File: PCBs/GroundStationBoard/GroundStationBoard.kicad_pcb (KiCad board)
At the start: 2 copper layers, 0 parts

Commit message: 4 layer-ifying the PCB, traces, board cuts and trace width
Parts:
- added A1: ADA3708, ADA3708:ADA3708_RPI-ZERO, F.Cu at (211.0, 52.0)
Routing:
- added copper zone on In2.Cu, net +5V
- added copper zone on B.Cu, net GND
- added copper zone on In1.Cu, net GND
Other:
- board outline added: 100 x 100 mm
- copper layers 2 -> 4

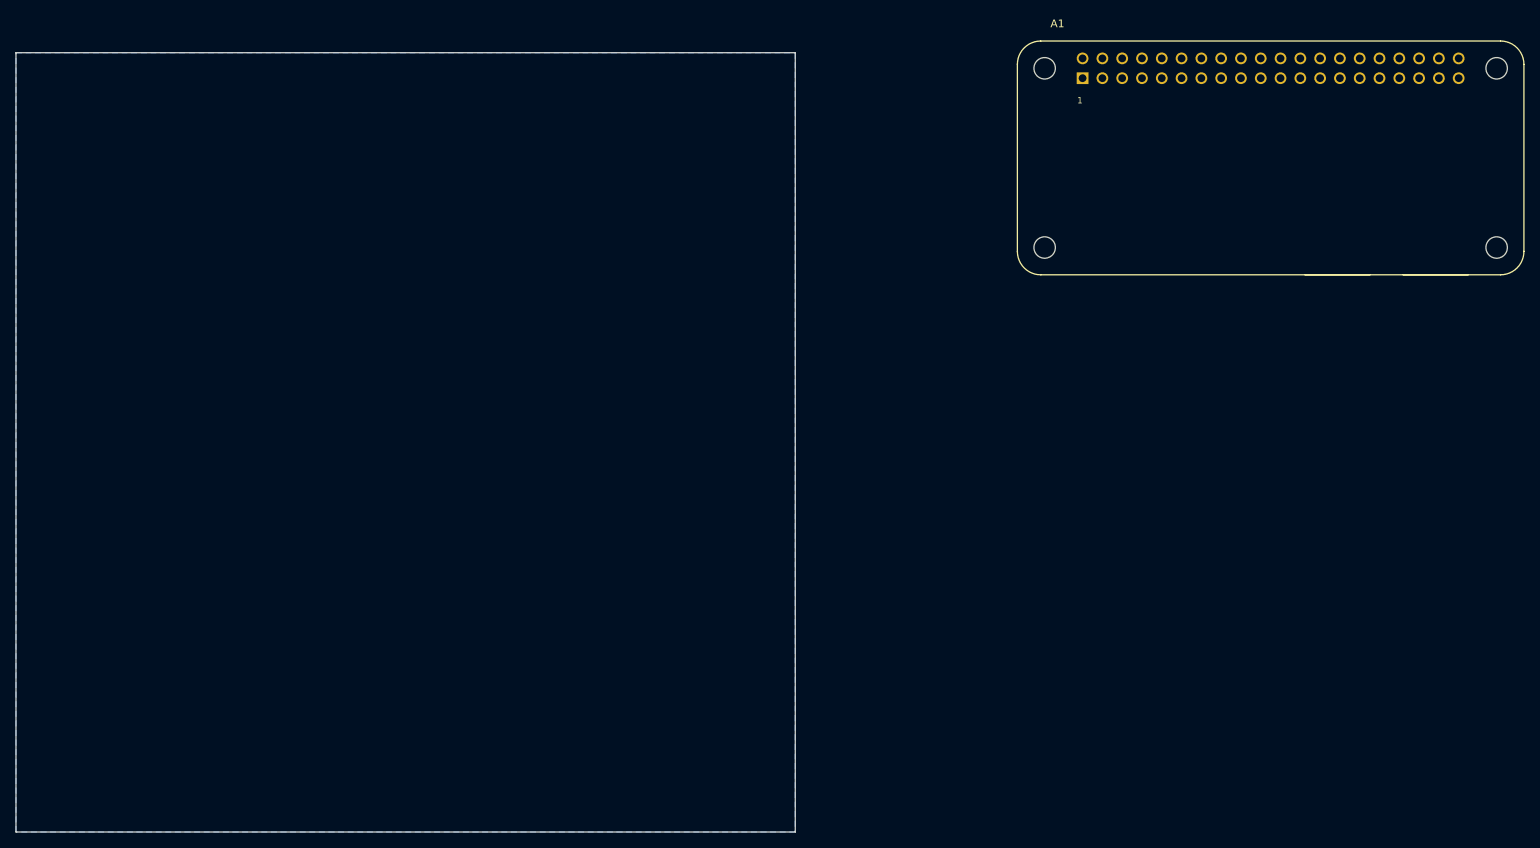
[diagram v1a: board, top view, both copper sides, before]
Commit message: added SMA connector and RF switch to schematic
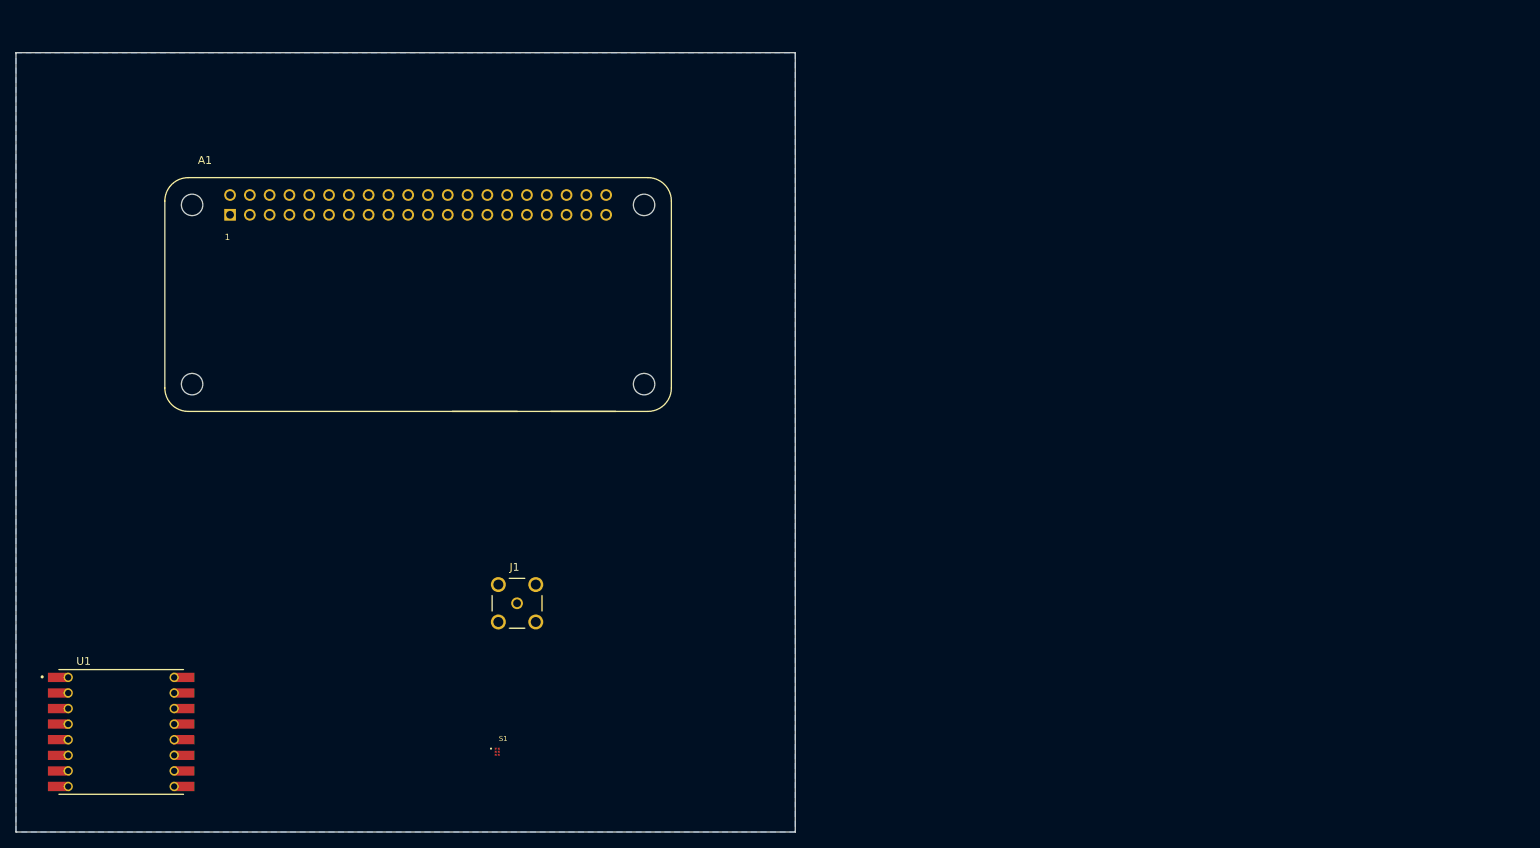
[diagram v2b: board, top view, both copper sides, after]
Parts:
- added J1: SMA_CONNECTOR, SMA_CONNECTOR:LPRS_SMA_CONNECTOR, F.Cu at (114.3, 120.7)
- added S1: BGS12P2L6E6327XTSA1, BGS12P2L6E6327XTSA1:SW_BGS12P2L6E6327XTSA1, F.Cu at (111.8, 139.7)
- added U1: RFM98W, RFM98W-433S2:XCVR_RFM98W-433S2, F.Cu at (63.5, 137.2)
- A1: value ADA3708 -> Raspberry Pi Zero
- moved A1 110.8 mm to (101.6, 69.5)
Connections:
- A1 pad 19: unconnected-(A1-Pad19) -> MOSI
- A1 pad 21: unconnected-(A1-Pad21) -> MISO
- A1 pad 23: unconnected-(A1-Pad23) -> SCLK
- A1 pad 24: unconnected-(A1-Pad24) -> CS
- A1 pad 40: unconnected-(A1-Pad40) -> RST

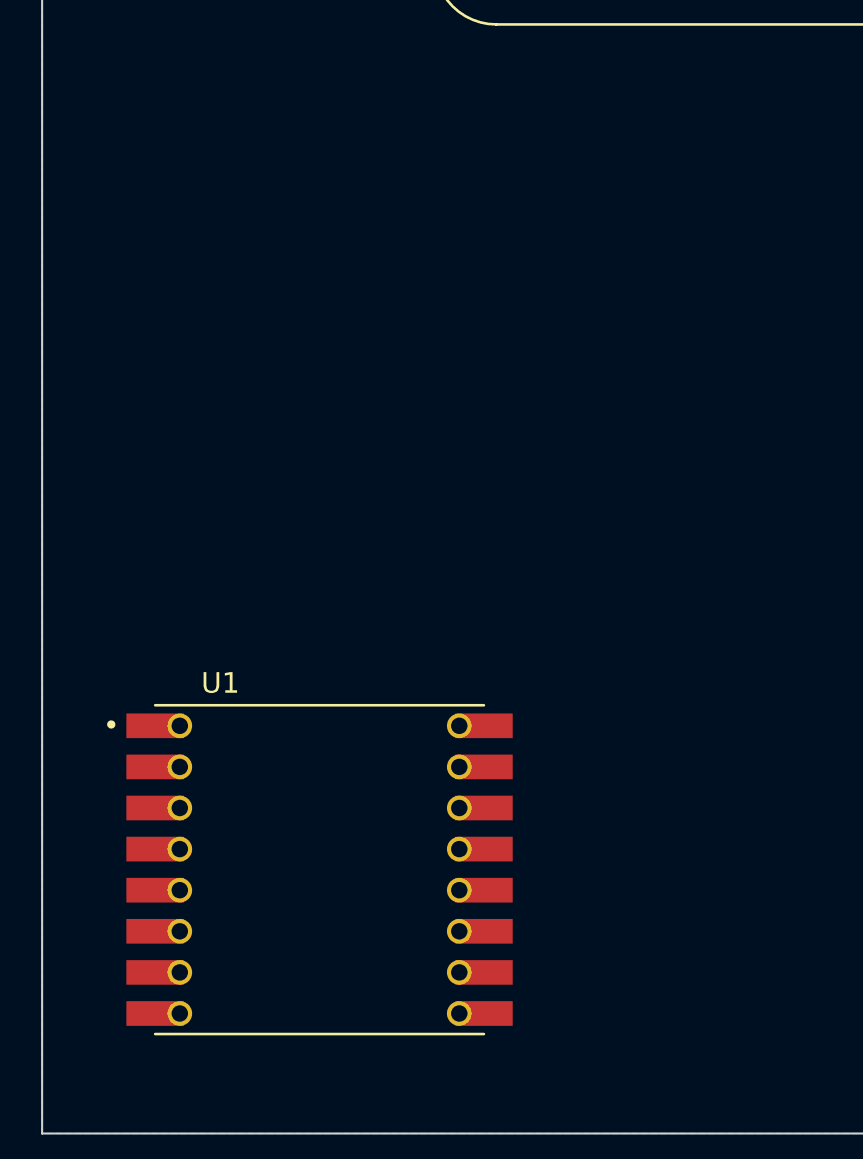
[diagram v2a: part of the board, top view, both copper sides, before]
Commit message: worked on data I/O pins
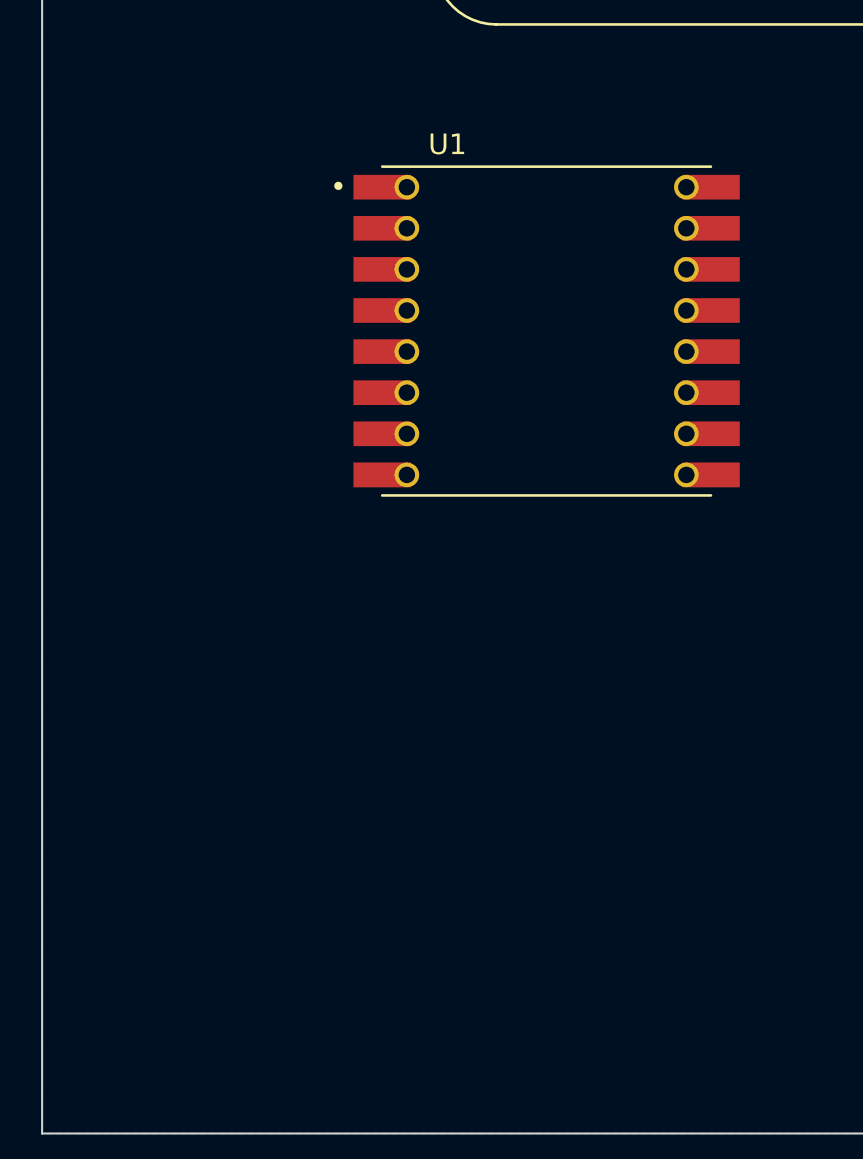
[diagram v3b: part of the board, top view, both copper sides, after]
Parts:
- moved U1 28.4 mm to (74.5, 111.0)
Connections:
- A1 pad 11: unconnected-(A1-Pad11) -> RST
- A1 pad 13: unconnected-(A1-Pad13) -> SWCH
- A1 pad 33: unconnected-(A1-Pad33) -> DIO0
- A1 pad 35: unconnected-(A1-Pad35) -> DIO1
- A1 pad 36: unconnected-(A1-Pad36) -> DIO3
- A1 pad 37: unconnected-(A1-Pad37) -> DIO2
- A1 pad 38: unconnected-(A1-Pad38) -> DIO4
- A1 pad 40: RST -> DIO5
- S1 pad 1: unconnected-(S1-Pad1) -> AMP
- S1 pad 3: unconnected-(S1-Pad3) -> ANT
- S1 pad 5: unconnected-(S1-Pad5) -> RF
- S1 pad 6: unconnected-(S1-Pad6) -> SWCH
- U1 pad 11: unconnected-(U1-Pad11) -> DIO3
- U1 pad 12: unconnected-(U1-Pad12) -> DIO4
- U1 pad 14: unconnected-(U1-Pad14) -> DIO0
- U1 pad 15: unconnected-(U1-Pad15) -> DIO1
- U1 pad 16: unconnected-(U1-Pad16) -> DIO2
- U1 pad 7: unconnected-(U1-Pad7) -> DIO5
- U1 pad 9: ANT -> RF

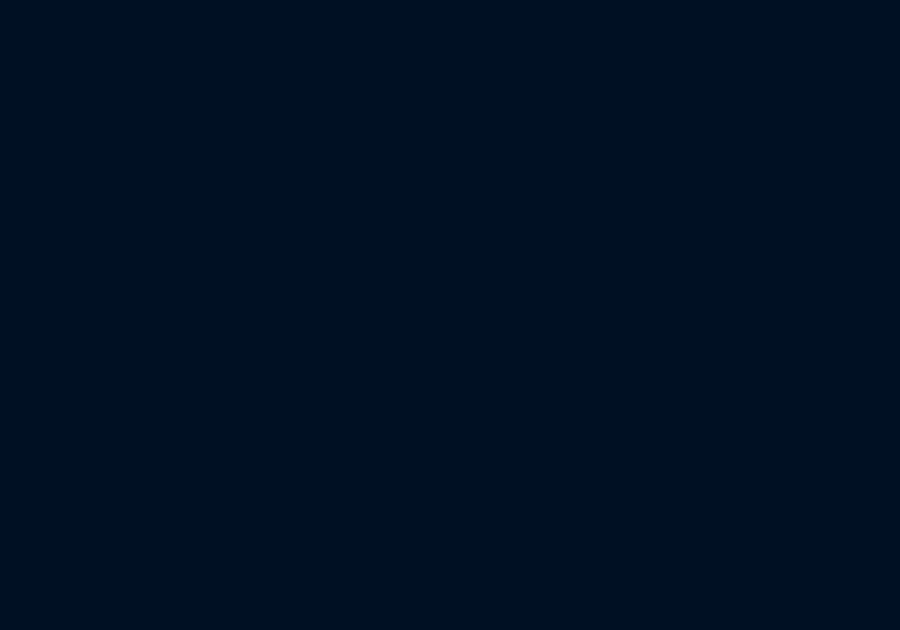
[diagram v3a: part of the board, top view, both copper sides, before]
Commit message: added amplifier
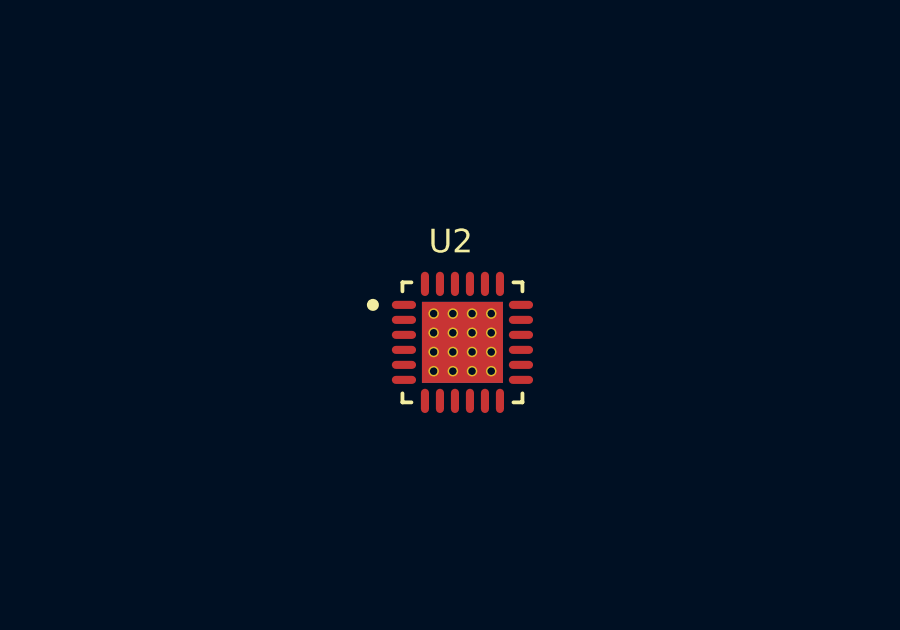
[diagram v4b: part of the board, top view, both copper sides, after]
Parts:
- added U2: TQP7M9106, TQP7M9106:QFN50P400X400X90-25N, F.Cu at (82.5, 135.9)
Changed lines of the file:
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@@
   (net 33 "DIO4")
   (net 34 "DIO5")
+  (net 35 "Net-(U2-Pad10)")
+  (net 36 "unconnected-(U2-Pad1)")
+  (net 37 "Net-(U2-Pad4)")
+  (net 38 "Net-(U2-Pad14)")
+  (net 39 "unconnected-(U2-Pad18)")
+  (net 40 "Net-(U2-Pad25)")
   (footprint "RFM98W-433S2:XCVR_RFM98W-433S2" (layer "F.Cu")
     (at 74.55 110.95)
@@
       (net 5 "GND") (pintype "passive"))
   )
+  (footprint "TQP7M9106:QFN50P400X400X90-25N" (layer "F.Cu")
+    (at 82.55 135.89)
+    (property "MANUFACTURER" "Qorvo")
+    (property "MAXIMUM_PACKAGE_HEIGHT" "0.9 mm")
+    (property "PARTREV" "Rev.D")
+    (property "SNAPEDA_PN" "TQP7M9106")
+    (property "STANDARD" "IPC-7351B")
+    (property "Sheetfile" "GroundStationBoard.kicad_sch")
+    (property "Sheetname" "")
+    (attr through_hole)
+    (fp_text reference "U2" (at -0.39 -3.365) (layer "F.SilkS")
+      (effects (font (size 0.787402 0.787402) (thickness 0.15)))
+    )
+    (fp_text value "TQP7M9106" (at 7.11 3.365) (layer "F.Fab")
+      (effects (font (size 0.787402 0.787402) (thickness 0.15)))
+    )
+    (fp_poly (pts
+        (xy -0.85 -0.85)
+        (xy 0.85 -0.85)
+        (xy 0.85 0.85)
+        (xy -0.85 0.85)
+      ) (layer "F.Paste") (width 0.01) (fill solid))
+    (fp_line (start -2 -2) (end -1.7 -2) (layer "F.SilkS") (width 0.127))
+    (fp_line (start 2 2) (end 1.7 2) (layer "F.SilkS") (width 0.127))
+    (fp_line (start -2 -2) (end -2 -1.7) (layer "F.SilkS") (width 0.127))
+    (fp_line (start 2 -2) (end 2 -1.7) (layer "F.SilkS") (width 0.127))
+    (fp_line (start -2 2) (end -1.7 2) (layer "F.SilkS") (width 0.127))
+    (fp_line (start -2 2) (end -2 1.7) (layer "F.SilkS") (width 0.127))
+    (fp_line (start 2 2) (end 2 1.7) (layer "F.SilkS") (width 0.127))
+    (fp_line (start 2 -2) (end 1.7 -2) (layer "F.SilkS") (width 0.127))
+    (fp_circle (center -2.985 -1.25) (end -2.885 -1.25) (layer "F.SilkS") (width 0.2) (fill none))
+    (fp_line (start 2.615 2.615) (end 2.615 -2.615) (layer "F.CrtYd") (width 0.05))
+    (fp_line (start -2.615 -2.615) (end 2.615 -2.615) (layer "F.CrtYd") (width 0.05))
+    (fp_line (start -2.615 2.615) (end -2.615 -2.615) (layer "F.CrtYd") (width 0.05))
+    (fp_line (start -2.615 2.615) (end 2.615 2.615) (layer "F.CrtYd") (width 0.05))
+    (fp_line (start 2 2) (end -2 2) (layer "F.Fab") (width 0.127))
+    (fp_line (start 2 2) (end 2 -2) (layer "F.Fab") (width 0.127))
+    (fp_line (start -2 2) (end -2 -2) (layer "F.Fab") (width 0.127))
+    (fp_line (start 2 -2) (end -2 -2) (layer "F.Fab") (width 0.127))
+    (fp_circle (center -2.985 -1.25) (end -2.885 -1.25) (layer "F.Fab") (width 0.2) (fill none))
+    (pad "1" smd oval locked (at -1.95 -1.25) (size 0.81 0.27) (layers "F.Cu" "F.Paste" "F.Mask")
+      (net 36 "unconnected-(U2-Pad1)") (pinfunction "VBIAS") (pintype "power_in"))
+    (pad "2" smd oval locked (at -1.95 -0.75) (size 0.81 0.27) (layers "F.Cu" "F.Paste" "F.Mask")
+      (net 35 "Net-(U2-Pad10)") (pinfunction "GND/NC") (pintype "power_in"))
+    (pad "3" smd oval locked (at -1.95 -0.25) (size 0.81 0.27) (layers "F.Cu" "F.Paste" "F.Mask")
+      (net 35 "Net-(U2-Pad10)") (pinfunction "GND/NC") (pintype "power_in"))
+    (pad "4" smd oval locked (at -1.95 0.25) (size 0.81 0.27) (layers "F.Cu" "F.Paste" "F.Mask")
+      (net 37 "Net-(U2-Pad4)") (pinfunction "RF_IN") (pintype "input"))
+    (pad "5" smd oval locked (at -1.95 0.75) (size 0.81 0.27) (layers "F.Cu" "F.Paste" "F.Mask")
+      (net 37 "Net-(U2-Pad4)") (pinfunction "RF_IN") (pintype "input"))
+    (pad "6" smd oval locked (at -1.95 1.25) (size 0.81 0.27) (layers "F.Cu" "F.Paste" "F.Mask")
+      (net 35 "Net-(U2-Pad10)") (pinfunction "GND/NC") (pintype "power_in"))
+    (pad "7" smd oval locked (at -1.25 1.95) (size 0.27 0.81) (layers "F.Cu" "F.Paste" "F.Mask")
+      (net 35 "Net-(U2-Pad10)") (pinfunction "GND/NC") (pintype "power_in"))
+    (pad "8" smd oval locked (at -0.75 1.95) (size 0.27 0.81) (layers "F.Cu" "F.Paste" "F.Mask")
+      (net 35 "Net-(U2-Pad10)") (pinfunction "GND/NC") (pintype "power_in"))
+    (pad "9" smd oval locked (at -0.25 1.95) (size 0.27 0.81) (layers "F.Cu" "F.Paste" "F.Mask")
+      (net 35 "Net-(U2-Pad10)") (pinfunction "GND/NC") (pintype "power_in"))
+    (pad "10" smd oval locked (at 0.25 1.95) (size 0.27 0.81) (layers "F.Cu" "F.Paste" "F.Mask")
+      (net 35 "Net-(U2-Pad10)") (pinfunction "GND/NC") (pintype "power_in"))
+    (pad "11" smd oval locked (at 0.75 1.95) (size 0.27 0.81) (layers "F.Cu" "F.Paste" "F.Mask")
+      (net 35 "Net-(U2-Pad10)") (pinfunction "GND/NC") (pintype "power_in"))
+    (pad "12" smd oval locked (at 1.25 1.95) (size 0.27 0.81) (layers "F.Cu" "F.Paste" "F.Mask")
+      (net 35 "Net-(U2-Pad10)") (pinfunction "GND/NC") (pintype "power_in"))
+    (pad "13" smd oval locked (at 1.95 1.25) (size 0.81 0.27) (layers "F.Cu" "F.Paste" "F.Mask")
+      (net 35 "Net-(U2-Pad10)") (pinfunction "GND/NC") (pintype "power_in"))
+    (pad "14" smd oval locked (at 1.95 0.75) (size 0.81 0.27) (layers "F.Cu" "F.Paste" "F.Mask")
+      (net 38 "Net-(U2-Pad14)") (pinfunction "RF_OUT/VCC") (pintype "output"))
+    (pad "15" smd oval locked (at 1.95 0.25) (size 0.81 0.27) (layers "F.Cu" "F.Paste" "F.Mask")
+      (net 38 "Net-(U2-Pad14)") (pinfunction "RF_OUT/VCC") (pintype "output"))
+    (pad "16" smd oval locked (at 1.95 -0.25) (size 0.81 0.27) (layers "F.Cu" "F.Paste" "F.Mask")
+      (net 38 "Net-(U2-Pad14)") (pinfunction "RF_OUT/VCC") (pintype "output"))
+    (pad "17" smd oval locked (at 1.95 -0.75) (size 0.81 0.27) (layers "F.Cu" "F.Paste" "F.Mask")
+      (net 35 "Net-(U2-Pad10)") (pinfunction "GND/NC") (pintype "power_in"))
+    (pad "18" smd oval locked (at 1.95 -1.25) (size 0.81 0.27) (layers "F.Cu" "F.Paste" "F.Mask")
+      (net 39 "unconnected-(U2-Pad18)") (pinfunction "I_REF") (pintype "input"))
+    (pad "19" smd oval locked (at 1.25 -1.95) (size 0.27 0.81) (layers "F.Cu" "F.Paste" "F.Mask")
+      (net 35 "Net-(U2-Pad10)") (pinfunction "GND/NC") (pintype "power_in"))
+    (pad "20" smd oval locked (at 0.75 -1.95) (size 0.27 0.81) (layers "F.Cu" "F.Paste" "F.Mask")
+      (net 35 "Net-(U2-Pad10)") (pinfunction "GND/NC") (pintype "power_in"))
+    (pad "21" smd oval locked (at 0.25 -1.95) (size 0.27 0.81) (layers "F.Cu" "F.Paste" "F.Mask")
+      (net 35 "Net-(U2-Pad10)") (pinfunction "GND/NC") (pintype "power_in"))
+    (pad "22" smd oval locked (at -0.25 -1.95) (size 0.27 0.81) (layers "F.Cu" "F.Paste" "F.Mask")
+      (net 35 "Net-(U2-Pad10)") (pinfunction "GND/NC") (pintype "power_in"))
+    (pad "23" smd oval locked (at -0.75 -1.95) (size 0.27 0.81) (layers "F.Cu" "F.Paste" "F.Mask")
+      (net 35 "Net-(U2-Pad10)") (pinfunction "GND/NC") (pintype "power_in"))
+    (pad "24" smd oval locked (at -1.25 -1.95) (size 0.27 0.81) (layers "F.Cu" "F.Paste" "F.Mask")
+      (net 35 "Net-(U2-Pad10)") (pinfunction "GND/NC") (pintype "power_in"))
+    (pad "25" smd rect locked (at 0 0) (size 2.7 2.7) (layers "F.Cu" "F.Mask")
+      (net 40 "Net-(U2-Pad25)") (pinfunction "RF/DC_GND") (pintype "power_in"))
+    (pad "26" smd rect locked (at 0 0) (size 2.7 2.7) (layers "B.Cu" "B.Mask")
+      (net 40 "Net-(U2-Pad25)") (pinfunction "RF/DC_GND") (pintype "power_in"))
+    (pad "27" thru_hole circle locked (at -0.96 -0.96) (size 0.35 0.35) (drill 0.25) (layers *.Cu))
+    (pad "28" thru_hole circle locked (at -0.32 -0.96) (size 0.35 0.35) (drill 0.25) (layers *.Cu))
+    (pad "29" thru_hole circle locked (at 0.32 -0.96) (size 0.35 0.35) (drill 0.25) (layers *.Cu))
+    (pad "30" thru_hole circle locked (at 0.96 -0.96) (size 0.35 0.35) (drill 0.25) (layers *.Cu))
+    (pad "31" thru_hole circle locked (at -0.96 -0.32) (size 0.35 0.35) (drill 0.25) (layers *.Cu))
+    (pad "32" thru_hole circle locked (at -0.32 -0.32) (size 0.35 0.35) (drill 0.25) (layers *.Cu))
+    (pad "33" thru_hole circle locked (at 0.32 -0.32) (size 0.35 0.35) (drill 0.25) (layers *.Cu))
+    (pad "34" thru_hole circle locked (at 0.96 -0.32) (size 0.35 0.35) (drill 0.25) (layers *.Cu))
+    (pad "35" thru_hole circle locked (at -0.96 0.32) (size 0.35 0.35) (drill 0.25) (layers *.Cu))
+    (pad "36" thru_hole circle locked (at -0.32 0.32) (size 0.35 0.35) (drill 0.25) (layers *.Cu))
+    (pad "37" thru_hole circle locked (at 0.32 0.32) (size 0.35 0.35) (drill 0.25) (layers *.Cu))
+    (pad "38" thru_hole circle locked (at 0.96 0.32) (size 0.35 0.35) (drill 0.25) (layers *.Cu))
+    (pad "39" thru_hole circle locked (at -0.96 0.96) (size 0.35 0.35) (drill 0.25) (layers *.Cu))
+    (pad "40" thru_hole circle locked (at -0.32 0.96) (size 0.35 0.35) (drill 0.25) (layers *.Cu))
+    (pad "41" thru_hole circle locked (at 0.32 0.96) (size 0.35 0.35) (drill 0.25) (layers *.Cu))
+    (pad "42" thru_hole circle locked (at 0.96 0.96) (size 0.35 0.35) (drill 0.25) (layers *.Cu))
+  )
   (footprint "ADA3708:ADA3708_RPI-ZERO" (layer "F.Cu")
